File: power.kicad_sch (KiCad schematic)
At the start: 12 parts, among them IC1 TPS63030DSK

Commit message: big commit with power and inputs
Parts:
- removed D1, D2: D_Schottky, symbol Device:D_Schottky
- removed IC1: TPS63030DSK, Package_SON:WSON-10-1EP_2.5x2.5mm_P0.5mm_EP1.2x2mm, symbol Regulator_Switching:TPS63030DSK
- removed L1: 1.5uH 190mA, symbol Device:L
- added D1, D2, D3: RB521S30, Diode_SMD:D_SOD-523, symbol user:RB521S30
- added D4: LAD52C03L01, Diode_SMD:D_SOD-523, symbol Device:D_TVS_Filled
- added D5: BZT52C3V6-TP, Diode_SMD:D_SOD-123F, symbol Diode:BZT52Bxx
- added IC1: TLV61070A, Package_TO_SOT_SMD:SOT-23-6, symbol user:TLV61070A
- added IC2: RT8096AHGJ5, Package_TO_SOT_SMD:SOT-23-5, symbol user:RT8096AHGJ5
- added L1: 1.5uH, symbol Device:L_Iron
- added L2: 2.2uH, symbol Device:L_Iron
- added Q1: SSM3J35AMFV, Package_TO_SOT_SMD:SOT-723, symbol Device:Q_PMOS_GSD
- added R3: 100k, Resistor_SMD:R_0805_2012Metric, symbol Device:R
- added R4: 18k, Resistor_SMD:R_0805_2012Metric, symbol Device:R
- added R5: 180R, Resistor_SMD:R_0805_2012Metric, symbol Device:R
- BAT1, BAT2: value AAA -> 0.9-1.5V AAA
- C1, C2, C3: footprint Capacitor_SMD:C_0805_2012Metric_Pad1.18x1.45mm_HandSolder -> Capacitor_SMD:C_0805_2012Metric; Type (none) -> X5R/X7R
- C4: value 0.1uF -> 10uF; footprint Capacitor_SMD:C_0805_2012Metric_Pad1.18x1.45mm_HandSolder -> Capacitor_SMD:C_0805_2012Metric; Type (none) -> X5R/X7R
- R1: value 1M -> 90k; footprint Resistor_SMD:R_0805_2012Metric_Pad1.20x1.40mm_HandSolder -> Resistor_SMD:R_0805_2012Metric
- R2: value 200k -> 20k; footprint Resistor_SMD:R_0805_2012Metric_Pad1.20x1.40mm_HandSolder -> Resistor_SMD:R_0805_2012Metric
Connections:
- net 3V_REG: now also D2.1 (K), D3.1 (K); no longer C2.1, C3.1, R1.1
- net GND: now also BAT1.2 (-), D4.1 (A1), IC1.2 (GND), IC2.2 (GND), R4.2, R5.2; no longer BAT2.2 (-)
- net at C4.1: now also D2.2 (A), IC1.5 (VOUT), R3.1
- net VUSB: now reaches C1.1
- net VUSB: now also IC2.1 (EN), IC2.4 (VIN)
- net at BAT1.1 (+): now also BAT2.2 (-)
- net at BAT2.1 (+): now also D1.2 (A), D4.2 (A2), D5.1 (K); no longer BAT1.2 (-)
- net at R1.2, R2.1: now also IC2.5 (FB)
- new net: IC1.1 (SW), L2.2
- new net: C3.1, IC1.3 (EN), IC1.6 (VIN), L2.1, Q1.3 (D)
- new net: IC1.4 (FB), R3.2, R4.1
- new net: C2.1, D3.2 (A), L1.2, Q1.1 (G), R1.1
- new net: D1.1 (K), Q1.2 (S)
- new net: D5.2 (A), R5.1
- new net: IC2.3 (LX), L1.1

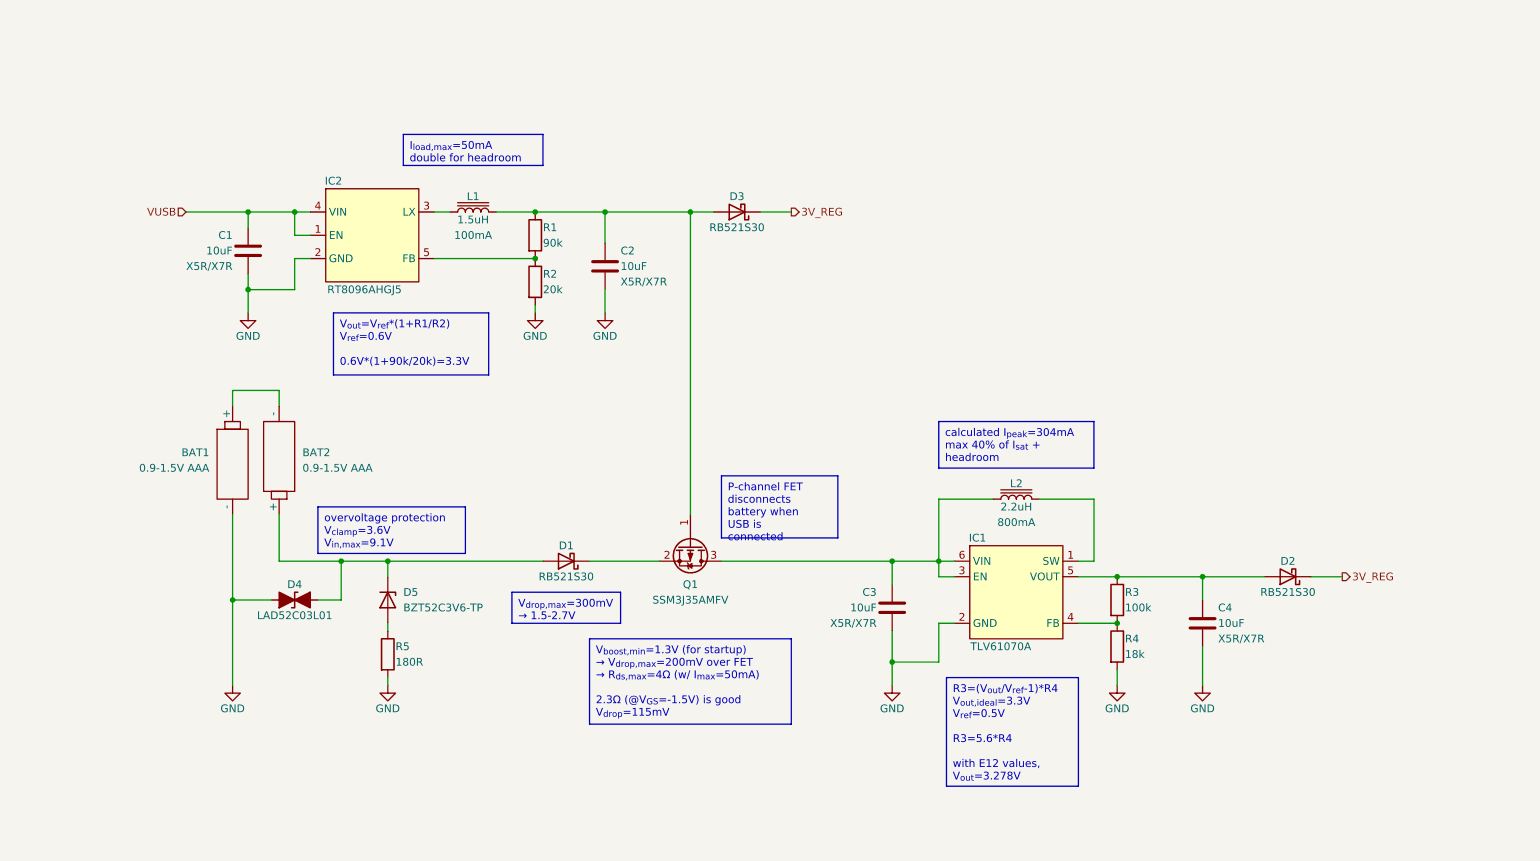
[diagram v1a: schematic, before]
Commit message: power supply cleanup and overvoltage protection
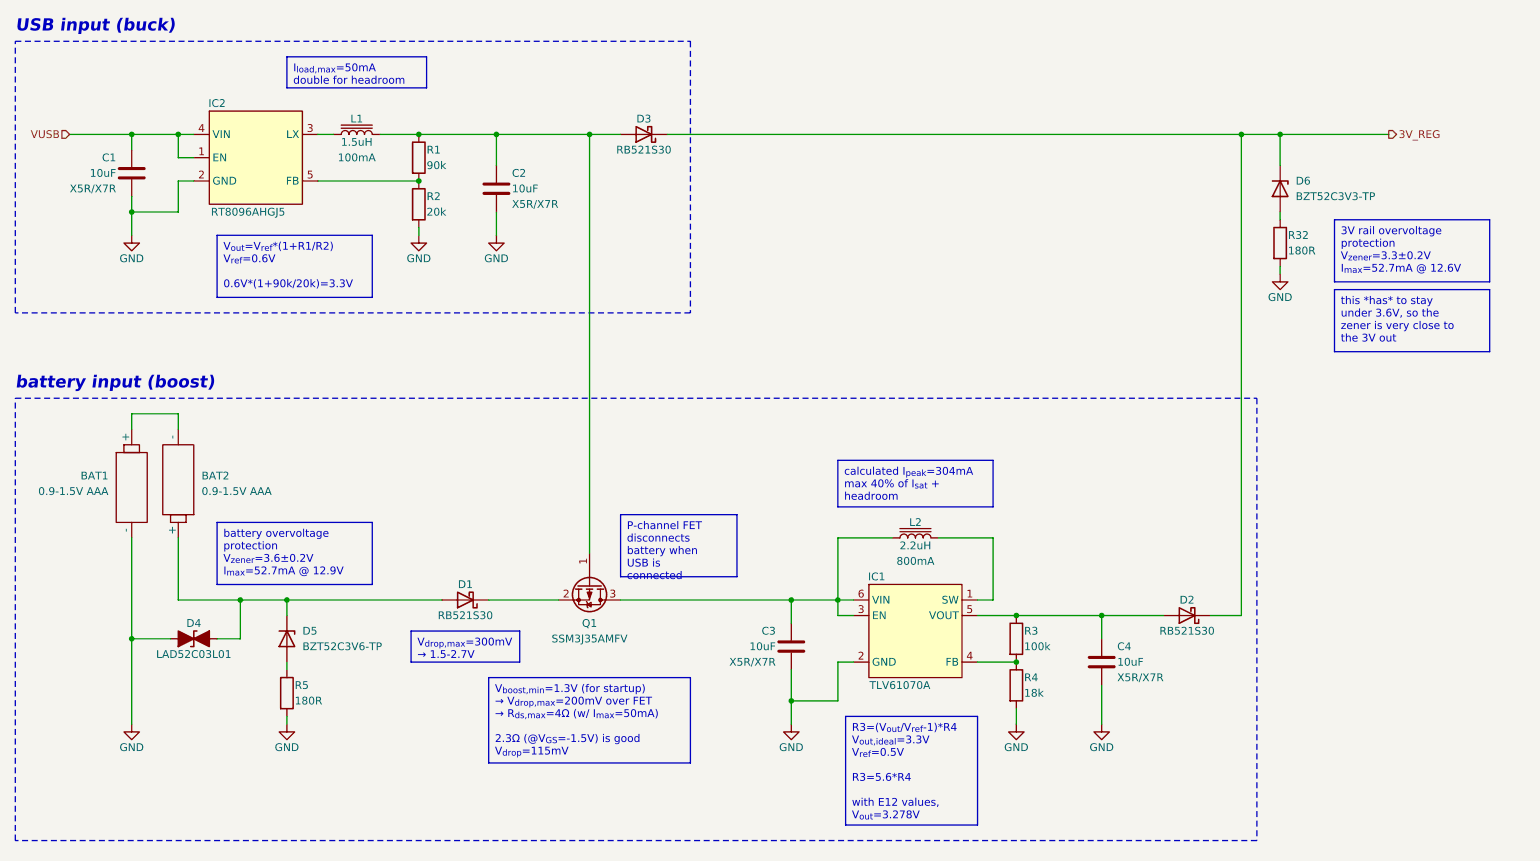
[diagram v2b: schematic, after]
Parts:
- added D6: BZT52C3V3-TP, Diode_SMD:D_SOD-123F, symbol Diode:BZT52Bxx
- added R32: 180R, Resistor_SMD:R_0805_2012Metric, symbol Device:R
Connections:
- net 3V_REG: now also D6.1 (K)
- net GND: now also R32.2
- new net: D6.2 (A), R32.1
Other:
- note added: "USB input (buck)"
- note added: "battery input (boost)"
- moved on the sheet: BAT1, BAT2, C1, C2, C3, C4, D1, D2, D3, D4, D5, IC1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

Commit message: added power ratings to overvoltage resistors
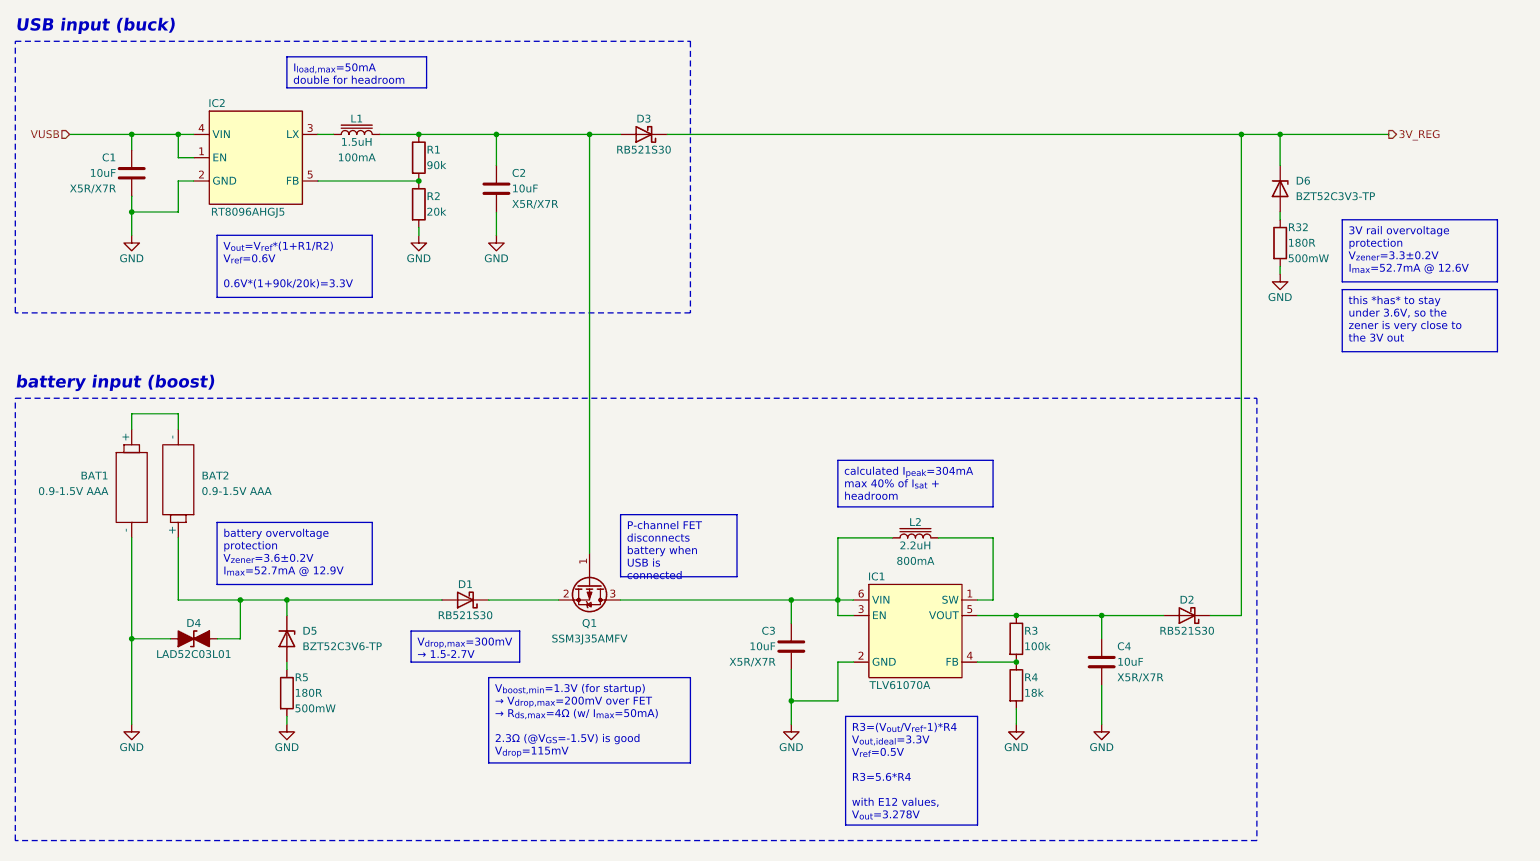
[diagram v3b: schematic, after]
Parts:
- R32, R5: Power (none) -> 500mW
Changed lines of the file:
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@@
   )
   (text_box "3V rail overvoltage protection\nV_{zener}=3.3±0.2V\nI_{max}=52.7mA @ 12.6V"
-    (at 245.11 60.96 0) (size 25.4 10.16)
+    (at 246.38 60.96 0) (size 25.4 10.16)
     (stroke (width 0) (type default) (color 132 0 0 1))
     (fill (type color) (color 255 255 194 1))
@@
   )
   (text_box "this *has* to stay under 3.6V, so the zener is very close to the 3V out"
-    (at 245.11 72.39 0) (size 25.4 10.16)
+    (at 246.38 72.39 0) (size 25.4 10.16)
     (stroke (width 0) (type default) (color 132 0 0 1))
     (fill (type color) (color 255 255 194 1))
@@
   (symbol (lib_id "Device:R") (at 73.66 138.43 0) (unit 1)
     (in_bom yes) (on_board yes) (dnp no)
-    (property "Reference" "R5" (at 74.93 137.16 0)
-      (effects (font (size 1.27 1.27)) (justify left))
-    )
-    (property "Value" "180R" (at 74.93 139.7 0)
+    (property "Reference" "R5" (at 74.93 135.89 0)
+      (effects (font (size 1.27 1.27)) (justify left))
+    )
+    (property "Value" "180R" (at 74.93 138.43 0)
       (effects (font (size 1.27 1.27)) (justify left))
     )
@@
     (property "Datasheet" "~" (at 73.66 138.43 0)
       (effects (font (size 1.27 1.27)) hide)
+    )
+    (property "Power" "500mW" (at 74.93 140.97 0)
+      (effects (font (size 1.27 1.27)) (justify left))
     )
     (pin "1")
@@
   (symbol (lib_id "Device:R") (at 236.22 64.77 0) (unit 1)
     (in_bom yes) (on_board yes) (dnp no)
-    (property "Reference" "R32" (at 237.49 63.5 0)
-      (effects (font (size 1.27 1.27)) (justify left))
-    )
-    (property "Value" "180R" (at 237.49 66.04 0)
+    (property "Reference" "R32" (at 237.49 62.23 0)
+      (effects (font (size 1.27 1.27)) (justify left))
+    )
+    (property "Value" "180R" (at 237.49 64.77 0)
       (effects (font (size 1.27 1.27)) (justify left))
     )
@@
       (effects (font (size 1.27 1.27)) hide)
     )
-    (pin "1")
+    (property "Power" "500mW" (at 237.49 67.31 0)
+      (effects (font (size 1.27 1.27)) (justify left))
+    )
+    (pin "1")

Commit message: schema functionally done
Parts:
- removed D5: BZT52C3V6-TP, Diode_SMD:D_SOD-123F, symbol Diode:BZT52Bxx
- removed D6: BZT52C3V3-TP, Diode_SMD:D_SOD-123F, symbol Diode:BZT52Bxx
- removed R32, R5: 180R, Resistor_SMD:R_0805_2012Metric, symbol Device:R
- R1: value 90k -> 90k 1%
- R2: value 20k -> 20k 1%
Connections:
- net 3V3_REG: now reaches C2.1, D3.2 (A), L1.2, Q1.1 (G), R1.1
- net 3V_REG renamed 3V0_REG
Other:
- moved on the sheet: BAT1, BAT2, C1, C2, C3, C4, D1, D2, D3, D4, IC1, IC2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

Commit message: reannotation
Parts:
- renumbered C1 to C2, C2 to C3, C3 to C4, C4 to C5, D4 to D2, D1 to D3, D3 to D4, D2 to D5, IC2 to IC1, IC1 to IC2, R1 to R3, R2 to R4, R3 to R5, R4 to R6

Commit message: change 0603 to 0805
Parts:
- L1: footprint (none) -> Inductor_SMD:L_1008_2520Metric
- L2: footprint (none) -> Inductor_SMD:L_Bourns_SRP7028A_7.3x6.6mm
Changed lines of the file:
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@@
       (effects (font (size 1.27 1.27)))
     )
-    (property "Footprint" "" (at 173.99 113.03 0)
+    (property "Footprint" "Inductor_SMD:L_Bourns_SRP7028A_7.3x6.6mm" (at 173.99 113.03 0)
       (effects (font (size 1.27 1.27)) hide)
     )
-    (property "Datasheet" "~" (at 173.99 113.03 0)
+    (property "Datasheet" "https://www.mouser.fi/datasheet/2/40/LMLPD-3165140.pdf" (at 173.99 113.03 0)
       (effects (font (size 1.27 1.27)) hide)
     )
@@
       (effects (font (size 1.27 1.27)))
     )
-    (property "Footprint" "" (at 110.49 46.99 0)
+    (property "Footprint" "Inductor_SMD:L_1008_2520Metric" (at 110.49 46.99 0)
       (effects (font (size 1.27 1.27)) hide)
     )
-    (property "Datasheet" "~" (at 110.49 46.99 0)
+    (property "Datasheet" "https://www.mouser.fi/datasheet/2/281/1/J_E_TE243A_0024-2303178.pdf" (at 110.49 46.99 0)
       (effects (font (size 1.27 1.27)) hide)
     )

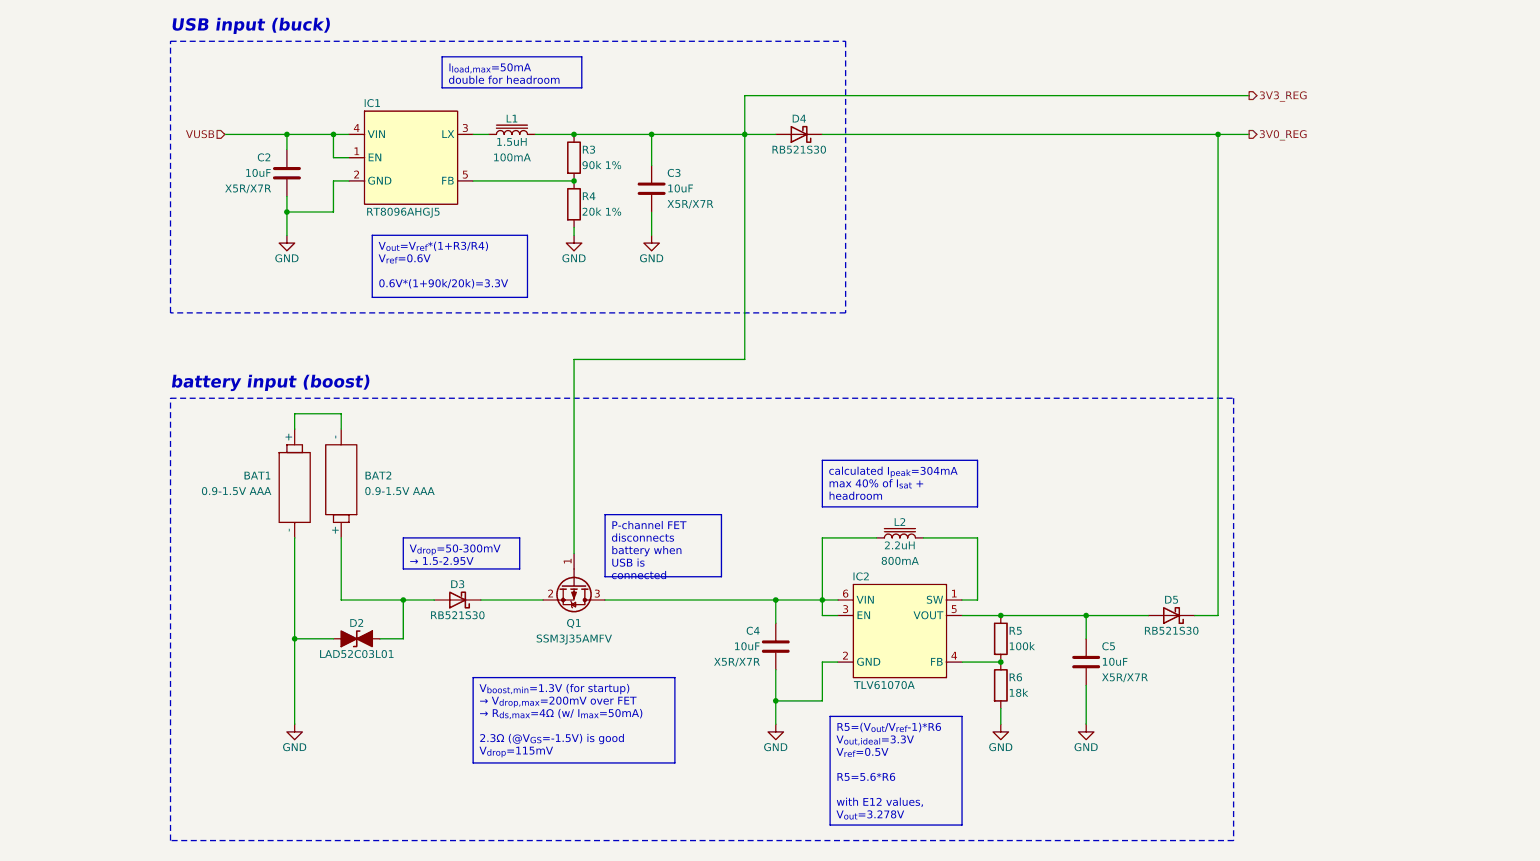
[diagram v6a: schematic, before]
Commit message: change usb buck resistor values
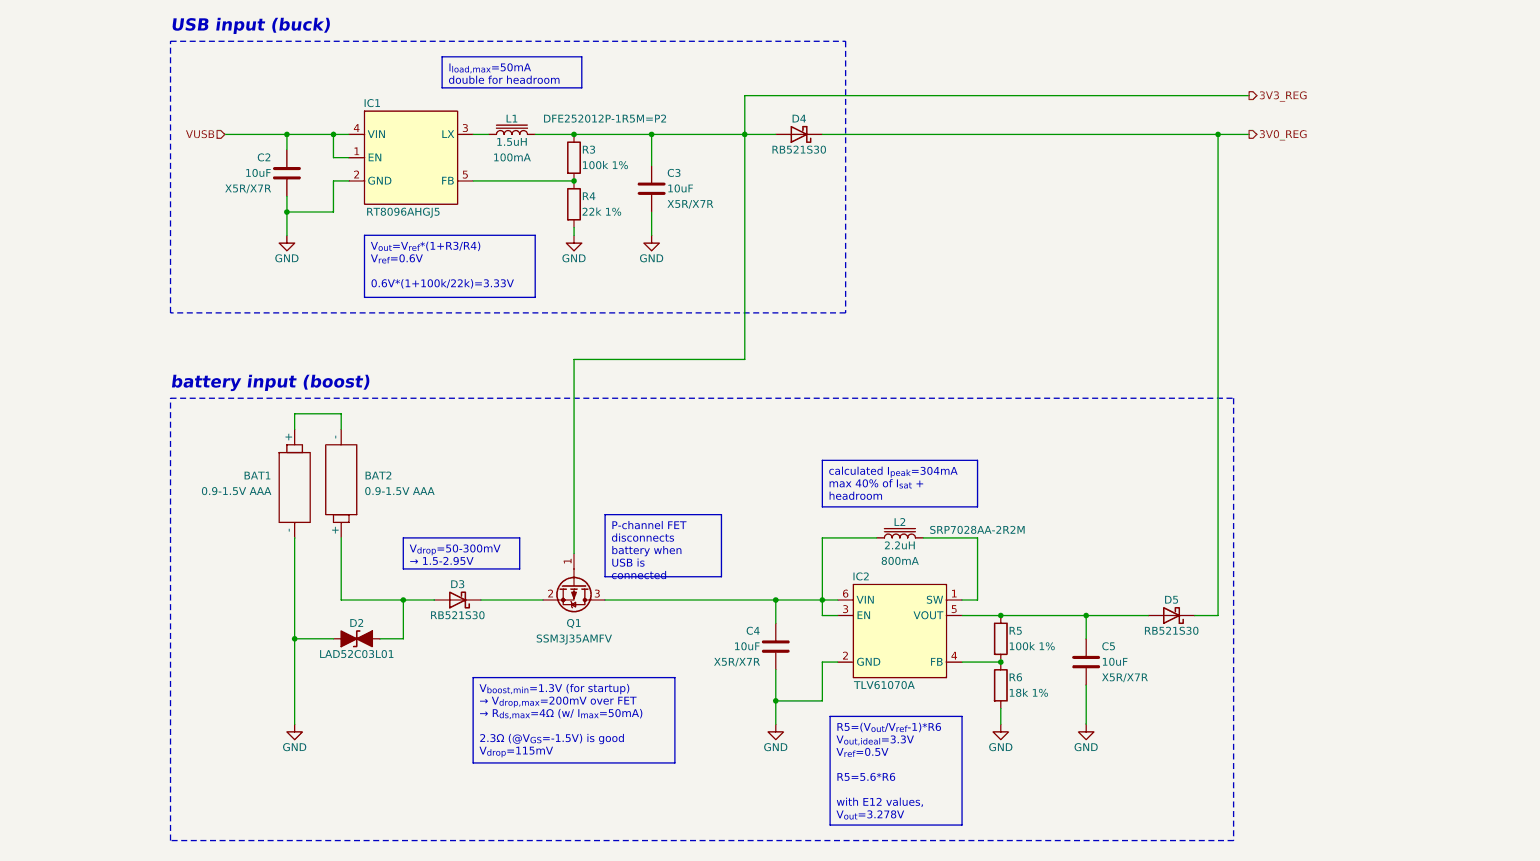
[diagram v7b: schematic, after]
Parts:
- L1: Model (none) -> DFE252012P-1R5M=P2
- L2: Model (none) -> SRP7028AA-2R2M
- R3: value 90k 1% -> 100k 1%
- R4: value 20k 1% -> 22k 1%
- R5: value 100k -> 100k 1%
- R6: value 18k -> 18k 1%
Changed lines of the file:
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@@
     (effects (font (size 1.27 1.27) (color 132 0 0 1)) (justify left top))
   )
-  (text_box "V_{out}=V_{ref}*(1+R3/R4)\nV_{ref}=0.6V\n\n0.6V*(1+90k/20k)=3.3V"
-    (at 87.63 63.5 0) (size 25.4 10.16)
+  (text_box "V_{out}=V_{ref}*(1+R3/R4)\nV_{ref}=0.6V\n\n0.6V*(1+100k/22k)=3.33V"
+    (at 86.36 63.5 0) (size 27.94 10.16)
     (stroke (width 0) (type default) (color 132 0 0 1))
     (fill (type color) (color 255 255 194 1))
@@
       (effects (font (size 1.27 1.27)) (justify left))
     )
-    (property "Value" "18k" (at 191.77 138.43 0)
+    (property "Value" "18k 1%" (at 191.77 138.43 0)
       (effects (font (size 1.27 1.27)) (justify left))
     )
@@
       (effects (font (size 1.27 1.27)) (justify left))
     )
-    (property "Value" "90k 1%" (at 121.92 52.07 0)
+    (property "Value" "100k 1%" (at 121.92 52.07 0)
       (effects (font (size 1.27 1.27)) (justify left))
     )
@@
       (effects (font (size 1.27 1.27)) hide)
     )
-    (property "Datasheet" "https://www.mouser.fi/datasheet/2/40/LMLPD-3165140.pdf" (at 173.99 113.03 0)
+    (property "Datasheet" "https://www.mouser.fi/datasheet/2/54/BOURNS_SRP7028AA-2064300.pdf" (at 173.99 113.03 0)
       (effects (font (size 1.27 1.27)) hide)
     )
     (property "Isat" "800mA" (at 173.99 116.84 90)
+      (effects (font (size 1.27 1.27)))
+    )
+    (property "Model" "SRP7028AA-2R2M" (at 186.69 111.76 90)
       (effects (font (size 1.27 1.27)))
     )
@@
       (effects (font (size 1.27 1.27)))
     )
+    (property "Model" "DFE252012P-1R5M=P2" (at 125.73 44.45 90)
+      (effects (font (size 1.27 1.27)))
+    )
     (pin "1")
     (pin "2")
@@
       (effects (font (size 1.27 1.27)) (justify left))
     )
-    (property "Value" "20k 1%" (at 121.92 59.69 0)
+    (property "Value" "22k 1%" (at 121.92 59.69 0)
       (effects (font (size 1.27 1.27)) (justify left))
     )
@@
       (effects (font (size 1.27 1.27)) (justify left))
     )
-    (property "Value" "100k" (at 191.77 130.81 0)
-      (effects (font (size 1.27 1.27)) (justify left))
-    )
+    (property "Value" "100k 1%" (at 191.77 130.81 0)
+      (effects (font (size 1.27 1.27)) (justify left))
+    )

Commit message: schematic cleanup
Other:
- moved on the sheet: BAT1, BAT2, C2, C3, D4, IC1, L1, R3, R4
